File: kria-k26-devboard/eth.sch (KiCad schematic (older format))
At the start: 39 parts, among them J1 5-2337992-8, Q1 BSS138DW-7-F, U1 DP83867CRRGZR

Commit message: fixed an issue with reset logic (Mixed PS and PL domain on OD buffer), extended the logic circuit to support M.2 PERST# (reset for PCIe WIFI), fixed the polarity of the camera control signal CAM_RST to comply with Antmicro standard, change CAM _SHDN to CAM_VSYNC, replaced the reset connector to fit additional signal M2_PERST
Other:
- note added: "Strap Configuration"
- moved on the sheet: C1, C10, C11, C12, C13, C14, C15, C16, C17, C18, C19, C2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

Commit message: Finished tidying up the schematic
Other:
- moved on the sheet: C1, C10, C11, C12, C13, C14, C15, C16, C17, C18, C19, C2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

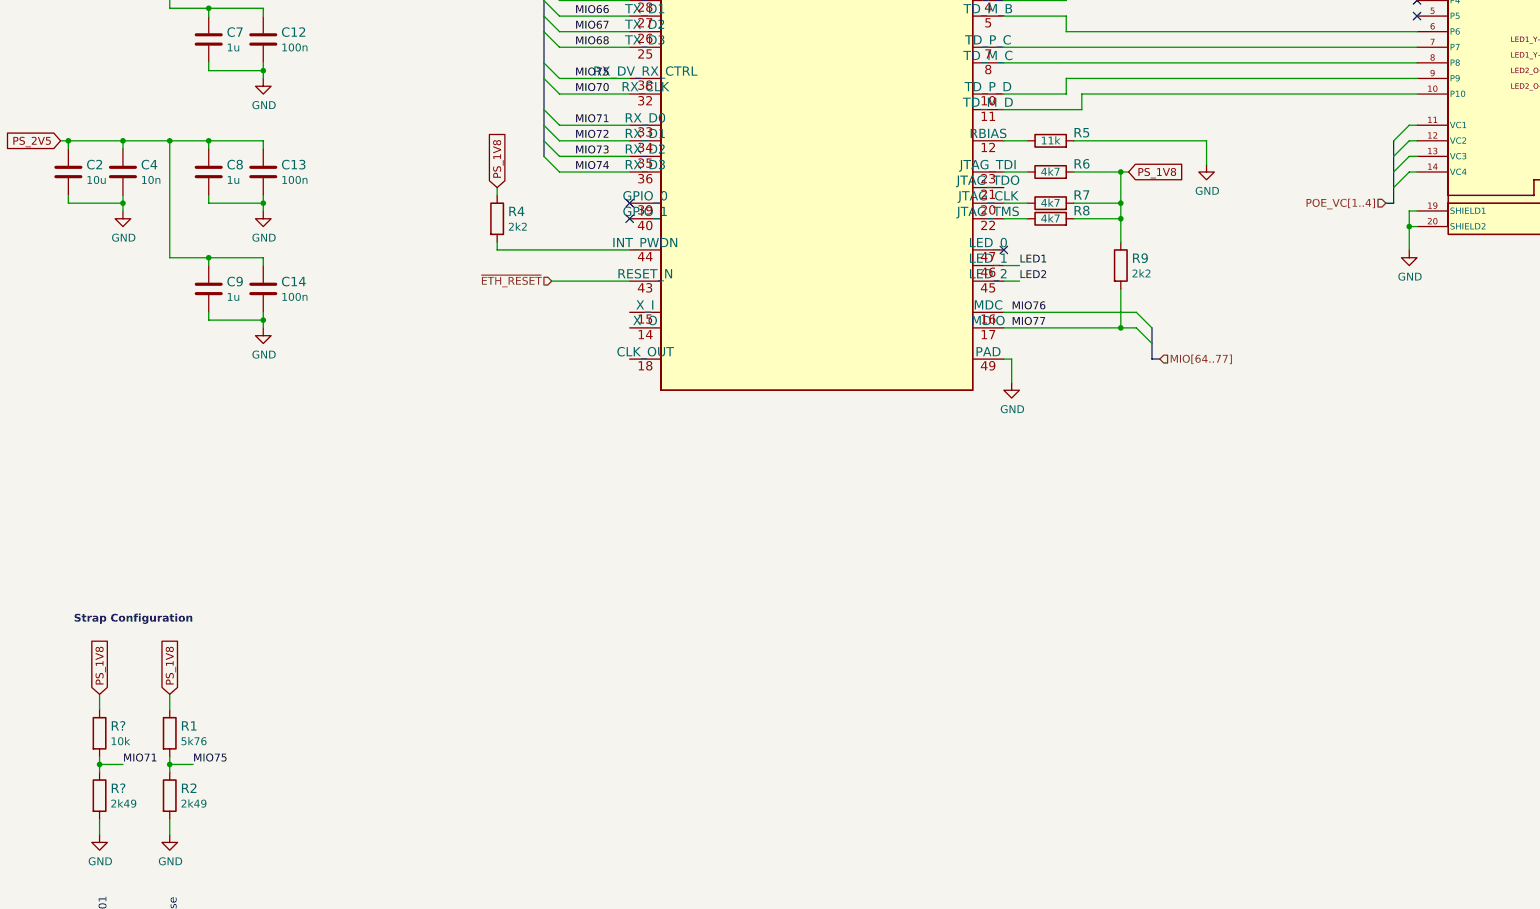
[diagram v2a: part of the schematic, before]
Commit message: Initial placement of power supply
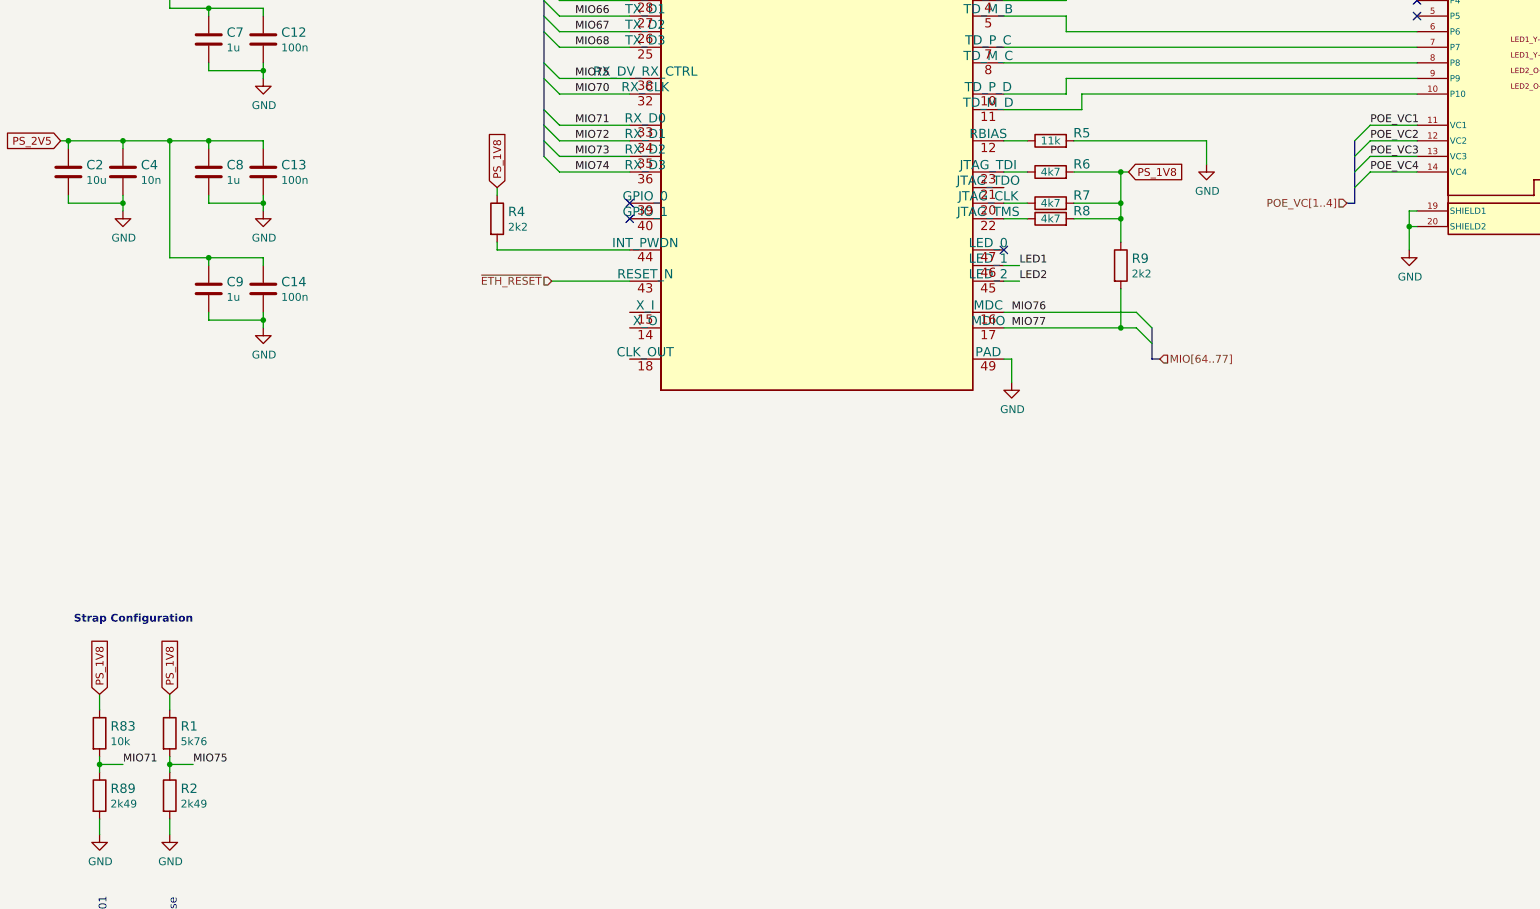
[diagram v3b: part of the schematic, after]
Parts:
- gave numbers to parts that had none: 2
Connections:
- net POE_VC1: now reaches J1.11 (VC1)
- net POE_VC2: now reaches J1.12 (VC2)
- net POE_VC3: now reaches J1.13 (VC3)
- net POE_VC4: now reaches J1.14 (VC4)
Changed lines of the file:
@@
 NoConn ~ 10200 3800
 NoConn ~ 10200 3900
-Text HLabel 10000 5100 0    50   Input ~ 0
+Text HLabel 9750 5100 0    50   Input ~ 0
 POE_VC[1..4]
 Wire Bus Line
-	10000 5100 10050 5100
+	9750 5100 9800 5100
 $Comp
 L antmicroModularConnectorsJacksWithMagnetics:5-2337992-8 J1
@@
 $EndComp
 Entry Wire Line
-	10050 5000 10150 4900
-Entry Wire Line
-	10050 4900 10150 4800
-Entry Wire Line
-	10050 4800 10150 4700
-Entry Wire Line
-	10050 4700 10150 4600
-Wire Wire Line
-	10150 4900 10200 4900
-Wire Wire Line
-	10150 4800 10200 4800
-Wire Wire Line
-	10150 4700 10200 4700
-Wire Wire Line
-	10150 4600 10200 4600
+	9800 5000 9900 4900
+Entry Wire Line
+	9800 4900 9900 4800
+Entry Wire Line
+	9800 4800 9900 4700
+Entry Wire Line
+	9800 4700 9900 4600
+Wire Wire Line
+	9900 4900 10200 4900
+Wire Wire Line
+	9900 4800 10200 4800
+Wire Wire Line
+	9900 4700 10200 4700
+Wire Wire Line
+	9900 4600 10200 4600
 Text HLabel 8550 6100 2    50   Input ~ 0
 MIO[64..77]
@@
 MIO75
 $Comp
-L antmicroResistors0402:R_10k_0402 R?
+L antmicroResistors0402:R_10k_0402 R83
 U 1 1 64F4CD3B
 P 1750 8500
-F 0 "R?" V 1705 8570 60  0000 L CNN
+F 0 "R83" V 1705 8570 60  0000 L CNN
 F 1 "R_10k_0402" H 1750 8350 60  0001 C CNN
 F 2 "antmicro-footprints:0402-res" H 1950 8700 60  0001 L CNN
@@
 	1750 8350 1750 8250
 $Comp
-L power:GND #PWR?
+L power:GND #PWR0349
 U 1 1 64F379D8
 P 1750 9150
-F 0 "#PWR?" H 1750 8900 50  0001 C CNN
+F 0 "#PWR0349" H 1750 8900 50  0001 C CNN
 F 1 "GND" H 1755 8977 50  0000 C CNN
 F 2 "" H 1750 9150 50  0001 C CNN
@@
 PS_1V8
 $Comp
-L antmicroResistors0402:R_2k49_0402 R?
+L antmicroResistors0402:R_2k49_0402 R89
 U 1 1 64F379C0
 P 1750 8900
-F 0 "R?" V 1705 8970 60  0000 L CNN
+F 0 "R89" V 1705 8970 60  0000 L CNN
 F 1 "R_2k49_0402" H 1750 8750 60  0001 C CNN
 F 2 "antmicro-footprints:0402-res" H 1950 9100 60  0001 L CNN
@@
 Text Notes 2350 7800 2    50   ~ 10
 Strap Configuration
+Text Label 9900 4600 0    50   ~ 0
+POE_VC1
+Text Label 9900 4700 0    50   ~ 0
+POE_VC2
+Text Label 9900 4800 0    50   ~ 0
+POE_VC3
+Text Label 9900 4900 0    50   ~ 0
+POE_VC4
 Wire Bus Line
 	8500 5900 8500 6100
 Wire Bus Line
-	10050 4700 10050 5100
+	9800 4700 9800 5100
 Wire Bus Line
 	4600 3250 4600 4800

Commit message: Progress in PCB placement
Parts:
- renumbered C21 to C100, C22 to C101, C23 to C102, C24 to C103, C1 to C80, C2 to C81, C3 to C82, C4 to C83, C5 to C84, C6 to C85, C7 to C86, C8 to C87, C9 to C88, C10 to C89, C11 to C90, C12 to C91, C13 to C92, C14 to C93, C15 to C94, C16 to C95, C17 to C96, C18 to C97, C19 to C98, C20 to C99, J1 to J5, Q1 to Q4, R83 to R45, R89 to R46, R1 to R47, R2 to R48, R4 to R49, R5 to R50, R6 to R51, R7 to R52, R8 to R53, R9 to R54, R10 to R55, R11 to R56, U1 to U21

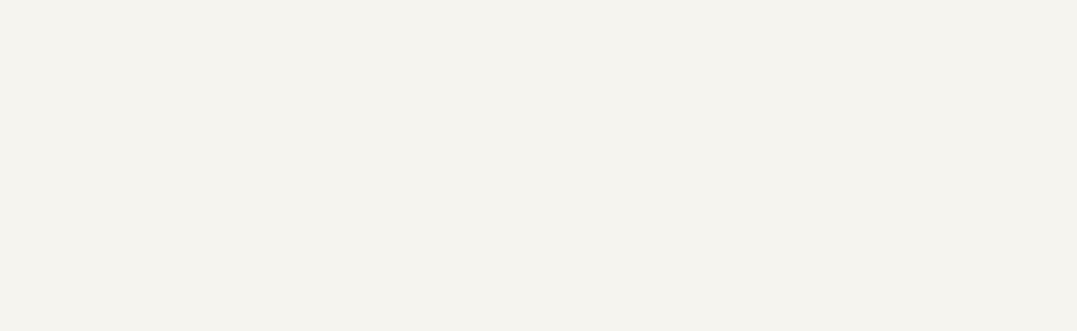
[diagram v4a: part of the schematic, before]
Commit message: PMOD, SD 3.0, PCIE and DP initial routing, optimized USB 2.0 and ETH signals routing
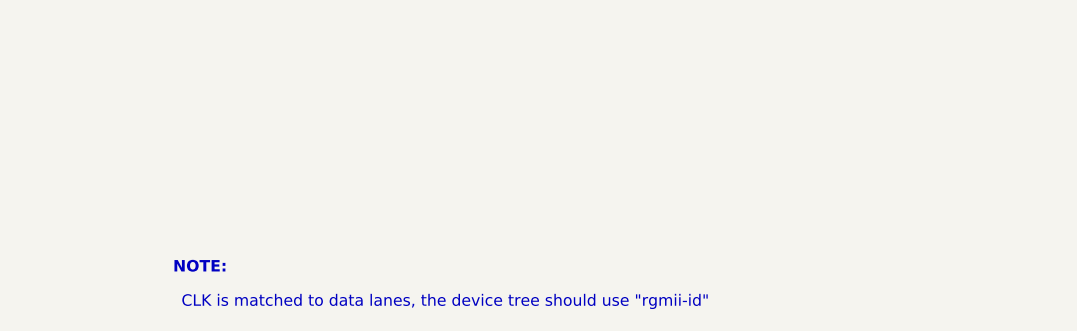
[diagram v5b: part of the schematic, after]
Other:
- note added: "CLK is matched to data lanes, the device tree should use "rgmii-id""
- note added: "NOTE:"
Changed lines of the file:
@@
 Wire Bus Line
 	4600 3250 4600 4800
+Text Notes 9050 11100 0    50   ~ 0
+CLK is matched to data lanes, the device tree should use "rgmii-id"
+Text Notes 9250 10950 2    50   ~ 10
+NOTE:
 $EndSCHEMATC

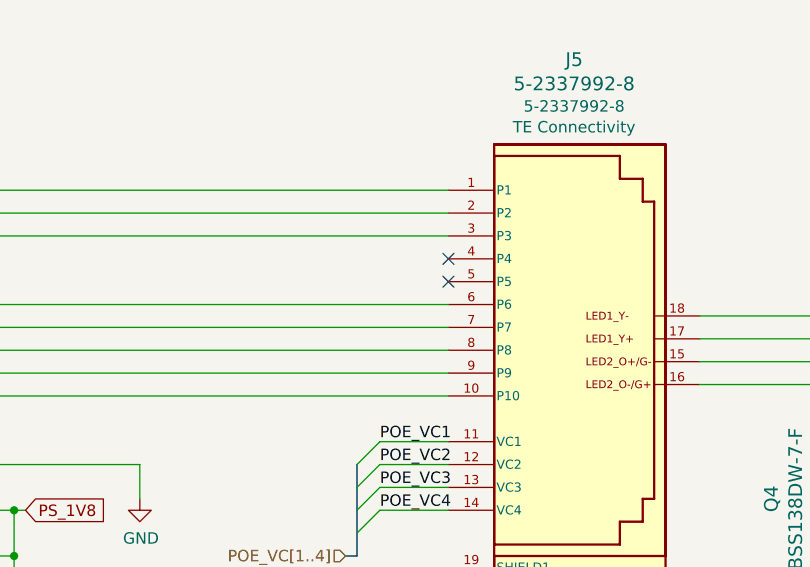
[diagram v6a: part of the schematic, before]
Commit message: Removed PL_1V2 DC-DC, Routed: signalling voltage selector for SD 3.0, reset signals and DC-DC enables, VSYNC, ETH connector diff. pairs, missing USB 3.0 diff. pair. Created planes for PoE adnd DC_MAIN_BUS
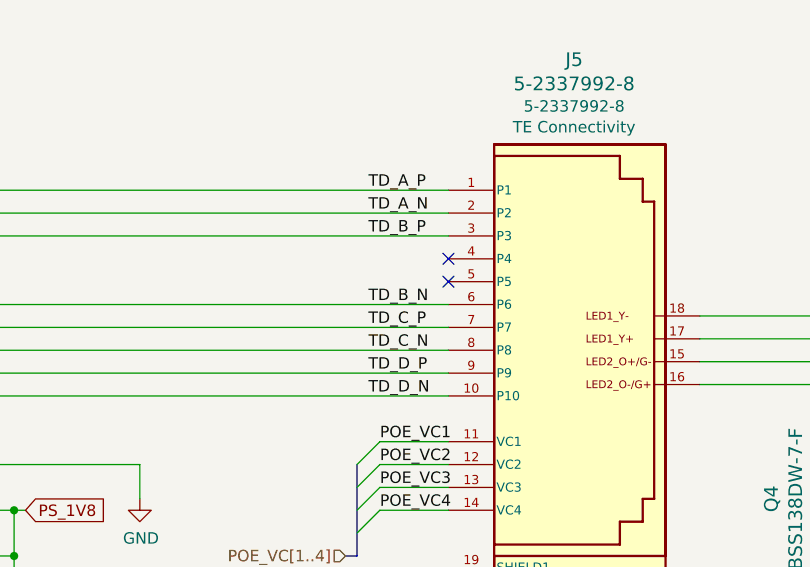
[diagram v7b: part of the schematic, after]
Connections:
- net TD_A_P: now reaches J5.1 (P1), U21.1 (TD_P_A)
- net TD_D_N: now reaches J5.10 (P10), U21.11 (TD_M_D)
- net TD_A_N: now reaches J5.2 (P2), U21.2 (TD_M_A)
- net TD_B_P: now reaches J5.3 (P3), U21.4 (TD_P_B)
- net TD_B_N: now reaches J5.6 (P6), U21.5 (TD_M_B)
- net TD_C_P: now reaches J5.7 (P7), U21.7 (TD_P_C)
- net TD_C_N: now reaches J5.8 (P8), U21.8 (TD_M_C)
- net TD_D_P: now reaches J5.9 (P9), U21.10 (TD_P_D)
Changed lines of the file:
@@
 Text Notes 9250 10950 2    50   ~ 10
 NOTE:
+Text Label 9850 3500 0    50   ~ 0
+TD_A_P
+Text Label 9850 3600 0    50   ~ 0
+TD_A_N
+Text Label 9850 3700 0    50   ~ 0
+TD_B_P
+Text Label 9850 4000 0    50   ~ 0
+TD_B_N
+Text Label 9850 4100 0    50   ~ 0
+TD_C_P
+Text Label 9850 4200 0    50   ~ 0
+TD_C_N
+Text Label 9850 4400 0    50   ~ 0
+TD_D_N
+Text Label 9850 4300 0    50   ~ 0
+TD_D_P
 Wire Bus Line
 	8500 5900 8500 6100

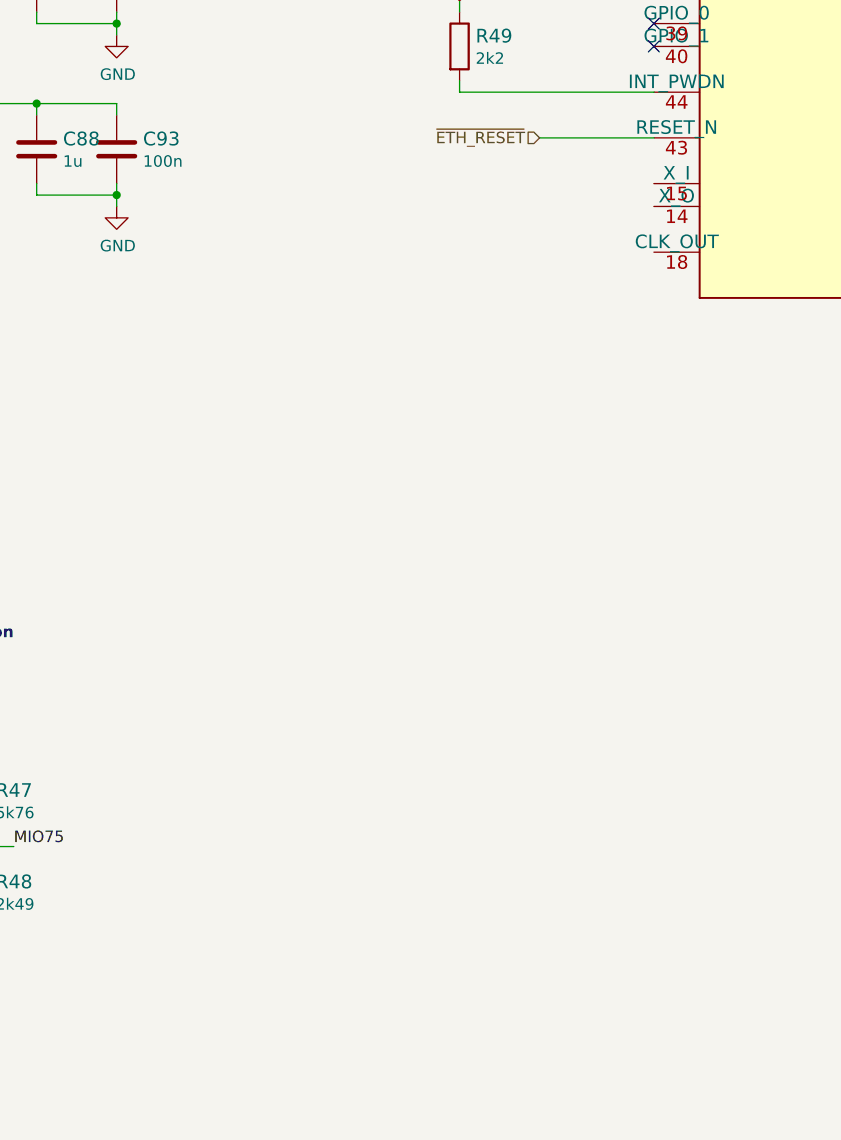
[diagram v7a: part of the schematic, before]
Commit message: Replaced PCIe clock generation (LVDS to HCSL), Clock component size optimization for USB, Optimized ESD protection for PD USB, placed and routed new clock circuitry, clock signals recalculated to 100Ohm  and re-routed
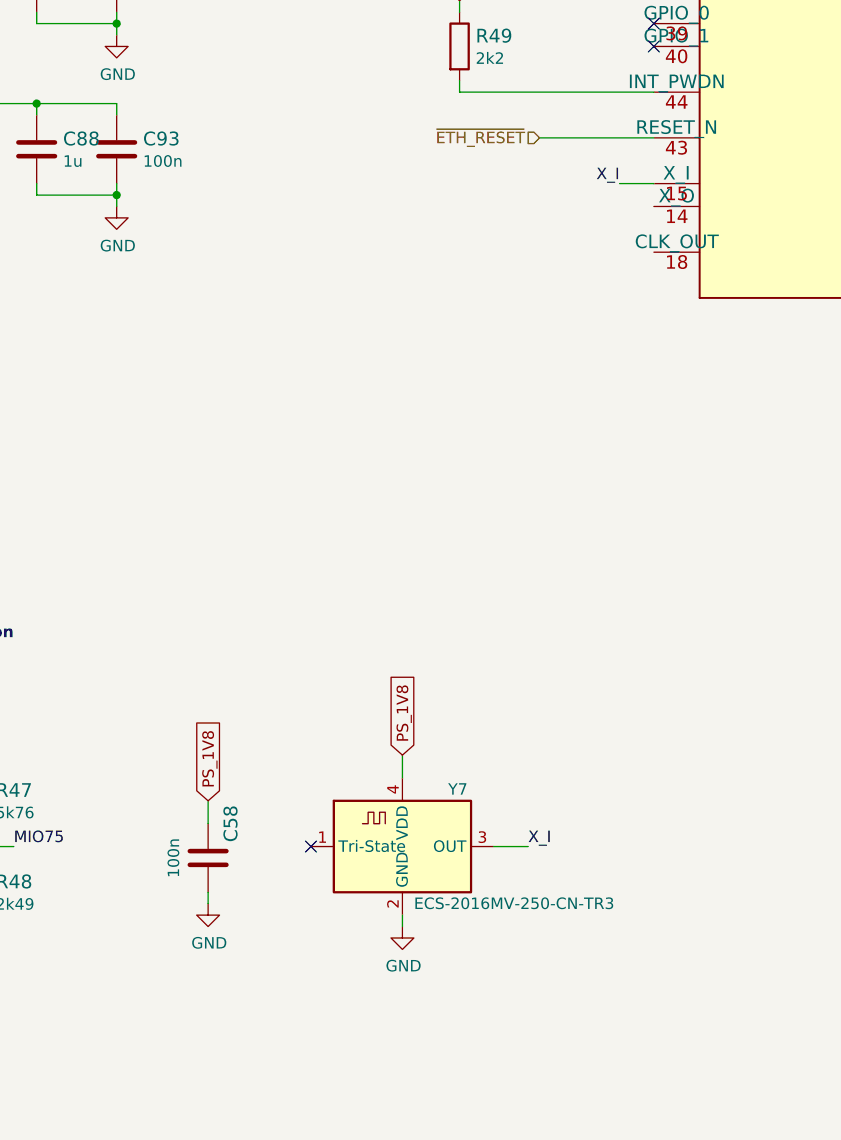
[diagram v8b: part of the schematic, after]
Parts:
- added C58: C_100n_0402, antmicro-footprints:0402-cap, symbol antmicroCapacitors0402:C_100n_0402
- added Y7: ECS-2016MV-250-CN-TR3, antmicro-footprints:ECS-2016MV, symbol antmicroCrystals:ECS-2016MV-250-CN-TR3
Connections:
- net GND: now also C58.1, Y7.2 (GND)
- net PS_1V8: now also C58.2, Y7.4 (VDD)
- net X_I: now reaches U21.15 (X_I)
- net X_I: now also Y7.3 (OUT)
- no-connect marks 7 -> 8
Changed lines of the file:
@@
 Text Label 9850 4300 0    50   ~ 0
 TD_D_P
+Wire Wire Line
+	4600 8700 4450 8700
+Wire Wire Line
+	4050 8400 4050 8300
+NoConn ~ 3650 8700
+$Comp
+L power:GND #PWR?
+U 1 1 6317DA6B
+P 4050 9050
+AR Path="/63CADD16/6317DA6B" Ref="#PWR?"  Part="1"
+AR Path="/63C3FA95/6317DA6B" Ref="#PWR0402"  Part="1"
+F 0 "#PWR0402" H 4050 8800 50  0001 C CNN
+F 1 "GND" H 4055 8877 50  0000 C CNN
+F 2 "" H 4050 9050 50  0001 C CNN
+F 3 "" H 4050 9050 50  0001 C CNN
+	1    4050 9050
+	1    0    0    -1
+$EndComp
+Wire Wire Line
+	4050 9050 4050 9000
+$Comp
+L power:GND #PWR?
+U 1 1 6317DA73
+P 3200 8950
+AR Path="/63CADD16/6317DA73" Ref="#PWR?"  Part="1"
+AR Path="/63C3FA95/6317DA73" Ref="#PWR0403"  Part="1"
+F 0 "#PWR0403" H 3200 8700 50  0001 C CNN
+F 1 "GND" H 3205 8777 50  0000 C CNN
+F 2 "" H 3200 8950 50  0001 C CNN
+F 3 "" H 3200 8950 50  0001 C CNN
+	1    3200 8950
+	1    0    0    -1
+$EndComp
+$Comp
+L antmicroCapacitors0402:C_100n_0402 C?
+U 1 1 6317DA7C
+P 3200 8750
+AR Path="/63CADD16/6317DA7C" Ref="C?"  Part="1"
+AR Path="/63C3FA95/6317DA7C" Ref="C58"  Part="1"
+F 0 "C58" V 3100 8600 60  0000 C CNN
+F 1 "C_100n_0402" H 3200 8600 60  0001 C CNN
+F 2 "antmicro-footprints:0402-cap" H 3400 8950 60  0001 L CNN
+F 3 "" H 3200 8750 50  0001 C CNN
+F 4 "Murata" H 3400 9150 60  0001 L CNN "Manufacturer"
+F 5 "GRM155R61H104KE14D" H 3400 9050 60  0001 L CNN "MPN"
+F 6 "100n" V 3350 8750 50  0000 C CNN "Val"
+	1    3200 8750
+	-1   0    0    1
+$EndComp
+Wire Wire Line
+	3200 8600 3200 8500
+Wire Wire Line
+	3200 8950 3200 8900
+$Comp
+L antmicroCrystals:ECS-2016MV-250-CN-TR3 Y?
+U 1 1 6317DA87
+P 4050 8700
+AR Path="/63CADD16/6317DA87" Ref="Y?"  Part="1"
+AR Path="/63C3FA95/6317DA87" Ref="Y7"  Part="1"
+F 0 "Y7" H 4250 8950 50  0000 L CNN
+F 1 "ECS-2016MV-250-CN-TR3" H 4100 8450 50  0000 L CNN
+F 2 "antmicro-footprints:ECS-2016MV" H 4500 8350 50  0001 C CNN
+F 3 "https://www.mouser.pl/datasheet/2/122/ECS_2016MV-2529299.pdf" H 3875 8825 50  0001 C CNN
+F 4 "ECS" H 4200 8250 50  0001 C CNN "Manufacturer"
+F 5 "ECS-2520MVLC-260-CM-TR" H 4700 8150 50  0001 C CNN "MPN"
+	1    4050 8700
+	1    0    0    -1
+$EndComp
+Text GLabel 4050 8300 1    50   Input ~ 0
+PS_1V8
+Text GLabel 3200 8500 1    50   Input ~ 0
+PS_1V8
+Text Label 5000 5800 2    50   ~ 0
+X_I
+Wire Wire Line
+	5000 5800 5150 5800
+Text Label 4600 8700 0    50   ~ 0
+X_I
 Wire Bus Line
 	8500 5900 8500 6100
